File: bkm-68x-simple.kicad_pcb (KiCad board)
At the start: 2 copper layers, 232 x 233.5 mm, 138 parts, among them CN985 mezz-conn-02x50, CN986 mezz-conn-02x50, J1 Y_G, J10 TP_VIDEO_OE, J11 TP_VSYNC, J12 JTAG, J13 USB_A, J2 PB_B, J3 PR_R, J4 EXT_SYNC, J5 TP_Y_G, J6 TP_PB_B, J7 TP_PR_R, J8 TP_HSYNC, J9 TP_INT_EXT_SYNC, SW1 SW_DIP_x04, SW2 FORCE_VIDEO, U1 ADG1611, U10 74LVC541A, U11 BA33BC0FP-E2, U12 TC7SZ125FU, U13 LM2990SX-5.0, U14 BA50BC0FP-E2, U2 THS7374, U3 ISL59885, U4 ADG734, U5 74LVC14A, U6 74LVC14A, U7 74LVC14A, U8 TC7WH125, U9 MAX10-EVAL

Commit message: Minor fixes and cleanups
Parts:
- C18: value 22uF -> 330uF/LOW_ESR; footprint Capacitor_SMD:CP_Elec_6.3x5.4 -> Capacitor_SMD:CP_Elec_6.3x7.7
- C19, C25, C28: value 1uF -> 10uF
- C24: value 33uF/LOW_ESR -> 100uF
- C26: footprint Capacitor_SMD:CP_Elec_6.3x5.4 -> Capacitor_SMD:CP_Elec_6.3x7.7
- C29: footprint Capacitor_SMD:CP_Elec_6.3x5.4 -> Capacitor_SMD:CP_Elec_6.3x5.8
- moved R24 21.9 mm to (245.4, 191.7), turned to 180 degrees
- moved R28 21.8 mm to (245.4, 197.6), turned to 180 degrees
- moved R26 18.2 mm to (245.4, 193.7), turned to 180 degrees
- moved R27 14.4 mm to (245.4, 195.6), turned to 180 degrees
- moved R29 9.61 mm to (245.4, 199.5), turned to 180 degrees
- moved R30 5.92 mm to (245.4, 201.4), turned to 180 degrees
- moved R32 3.59 mm to (240.4, 203.5)
- moved R31 2.30 mm to (245.4, 203.4), turned to 180 degrees
- moved C21 1.38 mm to (239.1, 191.4), turned to 180 degrees
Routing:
- net Net-(R29-Pad2): track 36.3 -> 4.75 mm
- net Net-(R32-Pad2): track 34.0 -> 2.46 mm
- net Net-(R28-Pad2): track 35.3 -> 4.22 mm, vias 2 -> 0
- net Net-(R27-Pad2): track 34.4 -> 4.74 mm
- net Net-(R26-Pad2): track 35.7 -> 6.03 mm
- net Net-(R24-Pad2): track 35.8 -> 7.48 mm
- net Net-(R30-Pad2): track 33.2 -> 5.72 mm
- net Net-(R31-Pad2): track 34.2 -> 7.16 mm
- net AD5: track 54.0 -> 81.1 mm
- net AD4: track 52.6 -> 78.5 mm
- net AD6: track 53.6 -> 78.7 mm
- net AD1: track 55.5 -> 80.0 mm
- net AD7: track 54.6 -> 79.0 mm
- net AD3: track 53.0 -> 77.4 mm, vias 1 -> 3
- net AD2: track 55.4 -> 79.7 mm
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
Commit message: A lotta fixes
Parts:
- removed R44, R45: R, Resistor_SMD:R_0805_2012Metric_Pad1.20x1.40mm_HandSolder
- removed SW1: SW_DIP_x04, Button_Switch_SMD:SW_DIP_SPSTx04_Slide_9.78x12.34mm_W8.61mm_P2.54mm
- added R71: 47R, Resistor_SMD:R_0805_2012Metric_Pad1.20x1.40mm_HandSolder, F.Cu at (261.6, 86.6)
- added R72: 47R, Resistor_SMD:R_0805_2012Metric_Pad1.20x1.40mm_HandSolder, F.Cu at (260.7, 89.9)
- J1: value Y_G -> PR_R
- J2: value PB_B -> Y_G
- J3: value PR_R -> PB_B
- U10: footprint Housings_SSOP:TSSOP-20_4.4x6.5mm_Pitch0.65mm -> Package_SO:TSSOP-20_4.4x6.5mm_P0.65mm
- U12: footprint Package_TO_SOT_SMD:SOT-23-5_HandSoldering -> Package_TO_SOT_SMD:SOT-353_SC-70-5_Handsoldering
- U4: footprint Package_SO:TSSOP-16_4.4x5mm_P0.65mm -> Package_SO:TSSOP-20_4.4x6.5mm_P0.65mm
- moved R42 74.0 mm to (141.9, 202.7), turned to 0 degrees
- moved R43 73.1 mm to (142.4, 197.8), turned to 90 degrees
- moved J10 23.6 mm to (237.7, 89.3)
- moved C8 5.35 mm to (199.1, 107.6)
- moved C18 2.84 mm to (249.2, 173.2), turned to 90 degrees
- moved J13 1.81 mm to (199.1, 143.4)
- moved C9 1.26 mm to (211.1, 107.1), turned to 180 degrees
- moved U12 0.19 mm to (235.9, 241.9)
- moved J11 0.19 mm to (264.2, 89.9)
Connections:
- C3 pad 2: Y_G_IN -> PR_R_IN
- C4 pad 2: PB_B_IN -> Y_G_IN
- C5 pad 2: PR_R_IN -> PB_B_IN
- D1 pad 2: PB_B_IN -> Y_G_IN
- D2 pad 1: PB_B_IN -> Y_G_IN
- D3 pad 2: PR_R_IN -> PB_B_IN
- D4 pad 1: PR_R_IN -> PB_B_IN
- D5 pad 2: Y_G_IN -> PR_R_IN
- D6 pad 1: Y_G_IN -> PR_R_IN
- J1 pad 1: Y_G_IN -> PR_R_IN
- J2 pad 1: PB_B_IN -> Y_G_IN
- J3 pad 1: PR_R_IN -> PB_B_IN
- R1 pad 2: PB_B_IN -> Y_G_IN
- R2 pad 2: PR_R_IN -> PB_B_IN
- R3 pad 2: Y_G_IN -> PR_R_IN
- R42 pad 1: FORCE_VIDEO_BIT3 -> Net-(R42-Pad1)
- R42 pad 2: Net-(R42-Pad2) -> HSYNC_SEP
- R43 pad 1: FORCE_VIDEO_BIT2 -> VSYNC_SEP
- R5 pad 2: HSYNC_SEP -> Net-(R42-Pad1)
- R6 pad 1: VSYNC_SEP -> Net-(R43-Pad2)
- R7 pad 1: HSYNC_SEP -> Net-(R42-Pad1)
- R8 pad 1: VSYNC_SEP -> Net-(R43-Pad2)
- U2 pad 9: GND -> +5VA
- U8 pad 3: VSYNC -> Net-(R72-Pad1)
- U8 pad 6: HSYNC -> Net-(R71-Pad1)
- U9 pad 43: FORCE_VIDEO_BIT3 -> (no net)
- U9 pad 46: FORCE_VIDEO_BIT2 -> (no net)
- U9 pad 47: FORCE_VIDEO_BIT1 -> (no net)
- U9 pad 55: FORCE_VIDEO_BIT0 -> (no net)
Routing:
- net HSYNC_SEP: track 150.3 -> 3.26 mm
- net Net-(R42-Pad1): track 0.00 -> 145.9 mm
- net VSYNC_SEP: track 143.1 -> 4.66 mm
- net Net-(R43-Pad2): track 8.01 -> 137.3 mm
- net FORCE_VIDEO_BIT2: track 89.1 -> 0.00 mm
- net FORCE_VIDEO_BIT3: track 89.1 -> 0.00 mm
- net FORCE_VIDEO_BIT1: track 89.1 -> 0.00 mm
- net FORCE_VIDEO_BIT0: track 89.1 -> 0.00 mm
- net +3V3: track 374.8 -> 363.1 mm, vias 11 -> 10
- net VSYNC: track 25.3 -> 16.9 mm
- net PR_R_IN: track 125.0 -> 133.1 mm
- net Net-(R45-Pad2): track 8.05 -> 0.00 mm
- net Net-(R44-Pad2): track 8.03 -> 0.00 mm
- net Net-(R42-Pad2): track 8.03 -> 0.00 mm
- net Y_G_IN: track 133.1 -> 125.8 mm
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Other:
- board text added: "PB/B (BLUE)"
- board text added: "PR/R (RED)"
- board text added: "Rev. A"
- board text added: "SYNC (YELLOW) Max 5Vpp"
- board text added: "Y/G (GREEN)"
- board text removed: "USB"

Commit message: Onboard FPGA, passthroughs and a lot of other stuff
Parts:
- added C30: 0.1uF, Capacitor_SMD:C_0603_1608Metric_Pad1.08x0.95mm_HandSolder, F.Cu at (213.0, 207.9)
- added C31: 0.1uF, Capacitor_SMD:C_0603_1608Metric_Pad1.08x0.95mm_HandSolder, F.Cu at (212.9, 211.2)
- added C32: 0.1uF, Capacitor_SMD:C_0603_1608Metric_Pad1.08x0.95mm_HandSolder, F.Cu at (212.7, 214.5)
- added C33: 0.1uF, Capacitor_SMD:C_0603_1608Metric_Pad1.08x0.95mm_HandSolder, F.Cu at (208.8, 219.8)
- added C34: 0.1uF, Capacitor_SMD:C_0603_1608Metric_Pad1.08x0.95mm_HandSolder, F.Cu at (210.3, 204.8)
- added C35: 0.1uF, Capacitor_SMD:C_0603_1608Metric_Pad1.08x0.95mm_HandSolder, F.Cu at (201.9, 196.6)
- added C36: 0.1uF, Capacitor_SMD:C_0603_1608Metric_Pad1.08x0.95mm_HandSolder, F.Cu at (206.1, 200.6)
- added C37: 0.1uF, Capacitor_SMD:C_0603_1608Metric_Pad1.08x0.95mm_HandSolder, F.Cu at (198.7, 194.6)
- added C38: 0.1uF, Capacitor_SMD:C_0603_1608Metric_Pad1.08x0.95mm_HandSolder, F.Cu at (190.3, 198.9)
- added C39: 0.1uF, Capacitor_SMD:C_0603_1608Metric_Pad1.08x0.95mm_HandSolder, F.Cu at (196.3, 194.5)
- added C40: 0.1uF, Capacitor_SMD:C_0603_1608Metric_Pad1.08x0.95mm_HandSolder, F.Cu at (185.5, 202.7)
- added C41: 0.1uF, Capacitor_SMD:C_0603_1608Metric_Pad1.08x0.95mm_HandSolder, F.Cu at (203.5, 223.5)
- added C42: 0.1uF, Capacitor_SMD:C_0603_1608Metric_Pad1.08x0.95mm_HandSolder, F.Cu at (200.3, 226.7)
- added C43: 0.1uF, Capacitor_SMD:C_0603_1608Metric_Pad1.08x0.95mm_HandSolder, F.Cu at (182.0, 215.6)
- added C44: 0.1uF, Capacitor_SMD:C_0603_1608Metric_Pad1.08x0.95mm_HandSolder, F.Cu at (185.9, 219.4)
- added C45: 0.1uF, Capacitor_SMD:C_0603_1608Metric_Pad1.08x0.95mm_HandSolder, F.Cu at (180.8, 214.5)
- added C46: 0.1uF, Capacitor_SMD:C_0603_1608Metric_Pad1.08x0.95mm_HandSolder, F.Cu at (180.5, 210.4)
- added C47: 0.1uF, Capacitor_SMD:C_0603_1608Metric_Pad1.08x0.95mm_HandSolder, F.Cu at (193.2, 226.9)
- added C48: 0.1uF, Capacitor_SMD:C_0603_1608Metric_Pad1.08x0.95mm_HandSolder, F.Cu at (191.3, 224.9)
- added C49: 0.1uF, Capacitor_SMD:C_0603_1608Metric_Pad1.08x0.95mm_HandSolder, F.Cu at (182.1, 206.7)
- added C50: 10pF, Capacitor_SMD:C_0603_1608Metric_Pad1.08x0.95mm_HandSolder, F.Cu at (185.2, 197.7)
- added C51: 10pF, Capacitor_SMD:C_0603_1608Metric_Pad1.08x0.95mm_HandSolder, F.Cu at (176.0, 201.1)
- added C52: 10pF, Capacitor_SMD:C_0603_1608Metric_Pad1.08x0.95mm_HandSolder, F.Cu at (188.4, 194.5)
- added C53: 10pF, Capacitor_SMD:C_0603_1608Metric_Pad1.08x0.95mm_HandSolder, F.Cu at (183.5, 199.4)
- added C54: 100pF, Capacitor_SMD:C_0805_2012Metric_Pad1.18x1.45mm_HandSolder, F.Cu at (202.3, 109.2)
- added C55: 470pF, Capacitor_SMD:C_0805_2012Metric_Pad1.18x1.45mm_HandSolder, F.Cu at (204.6, 109.2)
- added C56: 0.1uF, Capacitor_SMD:C_0805_2012Metric_Pad1.18x1.45mm_HandSolder, F.Cu at (262.0, 108.5)
- added C57: 0.1uF, Capacitor_SMD:C_0805_2012Metric_Pad1.18x1.45mm_HandSolder, F.Cu at (236.9, 111.2)
- added C58: 100uF, Capacitor_SMD:CP_Elec_6.3x5.4, F.Cu at (207.7, 187.4)
- added C59: 0.1uF, Capacitor_SMD:C_0805_2012Metric_Pad1.18x1.45mm_HandSolder, F.Cu at (204.5, 183.8)
- added D10: D_Schottky, Diode_SMD:D_SOD-123, F.Cu at (177.4, 199.7)
- added D11: D_Schottky, Diode_SMD:D_SOD-123, F.Cu at (185.4, 191.6)
- added D12: D_Schottky, Diode_SMD:D_SOD-123, F.Cu at (180.6, 196.5)
- added D13: DEBUG1, LED_SMD:LED_0805_2012Metric_Pad1.15x1.40mm_HandSolder, F.Cu at (182.0, 226.8)
- added D14: DEBUG2, LED_SMD:LED_0805_2012Metric_Pad1.15x1.40mm_HandSolder, F.Cu at (183.5, 228.4)
- added D9: D_Schottky, Diode_SMD:D_SOD-123, F.Cu at (182.3, 194.7)
- added J14: JTAG, Connector_PinHeader_2.54mm:PinHeader_2x05_P2.54mm_Vertical, F.Cu at (172.2, 193.5)
- added J15: Y_G_OUT, BNC-THT:BNC-THT, F.Cu at (57.8, 126.6)
- added J16: PB_B_OUT, BNC-THT:BNC-THT, F.Cu at (57.8, 166.7)
- added J17: EXT_SYNC_OUT, BNC-THT:BNC-THT, F.Cu at (57.7, 206.8)
- added Q1: MMBT3904, Package_TO_SOT_SMD:SOT-23_Handsoldering, F.Cu at (207.7, 110.0)
- added R44: 10K, Resistor_SMD:R_0805_2012Metric_Pad1.20x1.40mm_HandSolder, F.Cu at (205.6, 198.6)
- added R45: 10K, Resistor_SMD:R_0805_2012Metric_Pad1.20x1.40mm_HandSolder, F.Cu at (205.4, 194.8)
- added R73: 10K, Resistor_SMD:R_0805_2012Metric_Pad1.20x1.40mm_HandSolder, F.Cu at (204.0, 193.4)
- added R74: 10K, Resistor_SMD:R_0805_2012Metric_Pad1.20x1.40mm_HandSolder, F.Cu at (179.1, 198.2)
- added R75: 10K, Resistor_SMD:R_0805_2012Metric_Pad1.20x1.40mm_HandSolder, F.Cu at (187.0, 189.9)
- added R76: 1K, Resistor_SMD:R_0805_2012Metric_Pad1.20x1.40mm_HandSolder, F.Cu at (183.9, 193.2)
- added R77: 10K, Resistor_SMD:R_0805_2012Metric_Pad1.20x1.40mm_HandSolder, F.Cu at (182.0, 220.9)
- added R78: 22R, Resistor_SMD:R_0805_2012Metric_Pad1.20x1.40mm_HandSolder, F.Cu at (213.6, 194.3)
- added R79: 22R, Resistor_SMD:R_0805_2012Metric_Pad1.20x1.40mm_HandSolder, F.Cu at (211.1, 191.0)
- added R80: 100R, Resistor_SMD:R_0805_2012Metric_Pad1.20x1.40mm_HandSolder, F.Cu at (198.3, 110.9)
- added R81: 10K, Resistor_SMD:R_0805_2012Metric_Pad1.20x1.40mm_HandSolder, F.Cu at (206.8, 115.0)
- added R82: 470R, Resistor_SMD:R_0805_2012Metric_Pad1.20x1.40mm_HandSolder, F.Cu at (184.9, 223.9)
- added R83: 470R, Resistor_SMD:R_0805_2012Metric_Pad1.20x1.40mm_HandSolder, F.Cu at (186.4, 225.4)
- added SW1: FORCE_VIDEO, PTS645:PTS645, F.Cu at (53.3, 240.1)
- added SW3: PR_R_TERM, JS202011SCQN:JS202011SCQN, F.Cu at (77.2, 66.7)
- added SW4: Y_G_TERM, JS202011SCQN:JS202011SCQN, F.Cu at (77.1, 106.7)
- added SW5: PB_B_TERM, JS202011SCQN:JS202011SCQN, F.Cu at (77.0, 146.6)
- added SW6: EXT_SYNC_TERM, JS202011SCQN:JS202011SCQN, F.Cu at (77.0, 186.7)
- added U15: 10M08SC, Package_QFP:EQFP-144-1EP_20x20mm_P0.5mm_EP8.93x8.7mm_ThermalVias, F.Cu at (196.8, 210.9)
- C11: value 0.1uF -> 56nF
- C27: value C -> 0.1uF
- J13: value USB_A -> PR_R_OUT; footprint Connector_USB:USB_A_Molex_67643_Horizontal -> BNC-THT:BNC-THT
- R42, R43: value R -> 47R
- R46: value R -> 10K
- R5, R6, R7, R8: value R -> 1K
- U9: value MAX10-EVAL -> KC2520Z50; footprint max10-eval:max-10-eval -> Oscillator:Oscillator_SMD_Kyocera_KC2520Z-4Pin_2.5x2.0mm
- moved J13 152.0 mm to (58.0, 86.7), turned to 0 degrees
- moved C27 147.3 mm to (206.6, 122.2)
- moved R46 122.6 mm to (180.6, 219.4), turned to 225 degrees
- moved D8 60.1 mm to (69.9, 190.6)
- moved J4 60.0 mm to (57.7, 186.7)
- moved D7 60.0 mm to (69.9, 185.0)
- moved SW2 55.7 mm to (53.3, 229.8)
- moved R42 54.8 mm to (194.7, 187.8), turned to 225 degrees
- moved R43 52.1 mm to (193.2, 186.2), turned to 45 degrees
- moved R4 50.0 mm to (77.0, 180.6), turned to 0 degrees
- moved U9 47.0 mm to (182.0, 203.1), turned to 45 degrees
- moved D4 40.0 mm to (69.9, 150.6)
- moved J3 39.9 mm to (57.8, 146.6)
- moved D3 39.9 mm to (69.9, 145.0)
- moved R2 30.1 mm to (77.0, 140.5), turned to 0 degrees
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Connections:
- C10 pad 2: SYNC_SRC -> SYNC_SRC_FILTER
- C27 pad 1: FORCE_VIDEO -> +5VA
- J13 pad 1: STBY_5V -> Net-(J13-Pad1)
- J13 pad 2: (no net) -> GND
- R1 pad 1: GND -> Net-(R1-Pad1)
- R1 pad 2: Y_G_IN -> GND
- R2 pad 1: GND -> Net-(R2-Pad1)
- R2 pad 2: PB_B_IN -> GND
- R3 pad 1: GND -> Net-(R3-Pad1)
- R3 pad 2: PR_R_IN -> GND
- R4 pad 1: GND -> Net-(R4-Pad1)
- R4 pad 2: EXT_SYNC_IN -> GND
- R46 pad 2: Net-(R46-Pad2) -> +3V3
- SW2 pad 1: Net-(R46-Pad2) -> FORCE_VIDEO
- SW2 pad 2: +3V3 -> GND
- U1 pad 11: (no net) -> GND
- U1 pad 9: (no net) -> GND
- U3 pad 5: (no net) -> /Video/ISL_SD_HD
- U4 pad 10: (no net) -> GND
- U4 pad 11: (no net) -> GND
- U4 pad 12: (no net) -> GND
- U4 pad 14: (no net) -> GND
- U4 pad 17: (no net) -> GND
- U4 pad 19: (no net) -> GND
- U4 pad 20: (no net) -> GND
- U4 pad 7: (no net) -> GND
- U4 pad 9: (no net) -> GND
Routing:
- net +5VA: track 365.5 -> 532.4 mm
- net FORCE_VIDEO2: track 0.00 -> 146.7 mm
- net +3V3: track 363.1 -> 457.5 mm, vias 10 -> 21
- net STBY_5V: track 159.3 -> 69.1 mm
- net Net-(R42-Pad1): track 145.9 -> 67.2 mm
- net INT_~EXT~_SYNC: track 187.6 -> 113.2 mm, vias 2 -> 4
- net Net-(R43-Pad2): track 137.3 -> 67.2 mm
- net GND: track 97.6 -> 166.5 mm, vias 28 -> 53
- net VSYNC_OUT: track 180.1 -> 130.1 mm
- net HSYNC_OUT: track 176.3 -> 130.0 mm
- net FORCE_VIDEO: track 97.6 -> 140.3 mm
- net PB_B_IN: track 125.0 -> 158.7 mm
- net Y_G_IN: track 125.8 -> 158.5 mm
- net /FPGA/TCK: track 0.00 -> 27.9 mm
- net /FPGA/TMS: track 0.00 -> 27.4 mm
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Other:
- outline, holes or cut-outs redrawn
- board text added: "BKM-68X Alternative (SKM-69X) (2021) Martin Hejnfelt www.immerhax.com"
- board text added: "DBG1"
- board text added: "DBG2"
- board text added: "EXT. SYNC (YELLOW) Max 5Vpp"
- board text added: "EXT. SYNC OUT"
- board text added: "PB/B OUT"
- board text added: "PR/R OUT"
- board text added: "Rev. B"
- board text added: "UP = 75R TERM DOWN = PASSTHROUGH"
- board text added: "Y/G OUT"
- board text removed: "5V power only for FPGA"
- board text removed: "Altera/Intel MAX10 10M08S Evaluation Kit"
- board text removed: "BKM-68X Alternative (2021) Martin Hejnfelt www.immerhax.com"
- board text removed: "Rev. A"
- board text removed: "SYNC (YELLOW) Max 5Vpp"

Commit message: Updated some component values
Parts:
- R15, R16, R17, R18, R19, R20, R21, R22, R23, R25, R36, R38, R47, R48, R49, R50, R51, R52, R53, R62, R63, R64, R65, R66, R67: value 68 -> 68R
- R24, R26, R27, R28, R29, R30, R31, R32: value 47 -> 47R
- R40, R41, R54, R55, R56, R57, R58, R59, R60, R61, R68, R69, R70: value 22 -> 22R
- R83: value 470R -> 390R

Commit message: Fixes and additions
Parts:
- added C60: 0.1uF, Capacitor_SMD:C_0603_1608Metric_Pad1.08x0.95mm_HandSolder, F.Cu at (184.7, 218.3)
- added H1: SCREWMOUNT_90DEG, keystone-7794:7794-X, F.Cu at (57.5, 255.0)
- added H2: SCREWMOUNT_90DEG, keystone-7794:7794-X, F.Cu at (57.5, 45.0)
- moved C28 12.6 mm to (245.5, 100.5)
- moved C25 4.21 mm to (249.1, 120.4), turned to 270 degrees
- moved C19 1.74 mm to (253.8, 174.3), turned to 90 degrees
- moved C16 1.65 mm to (258.1, 126.7)
- moved C17 1.65 mm to (253.3, 126.4)
- moved C46 0.41 mm to (180.7, 210.7)
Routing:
- net -6V: track 118.9 -> 116.5 mm
- net +3V3: track 457.5 -> 459.9 mm
- net +6V: track 100.1 -> 98.7 mm
- net +5VA: track 532.4 -> 532.9 mm
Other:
- board text added: "Rev. C"
- board text removed: "Rev. B"

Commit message: Shortened board slightly for PCB front, rev C
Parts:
- moved J4 1.72 mm to (59.4, 186.6)
- moved J17 1.71 mm to (59.4, 206.6)
- moved J16 1.66 mm to (59.4, 166.6)
- moved J3 1.65 mm to (59.4, 146.6)
- moved J15 1.65 mm to (59.4, 126.6)
- moved H2 1.63 mm to (59.1, 45.0)
- moved H1 1.63 mm to (59.1, 255.0)
- moved SW2 1.51 mm to (54.8, 229.8)
- moved SW1 1.50 mm to (54.8, 240.1)
- moved J2 1.40 mm to (59.4, 106.7)
- moved J1 1.30 mm to (59.3, 66.7)
- moved J13 1.17 mm to (59.2, 86.7)
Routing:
- net Net-(J17-Pad1): track 25.0 -> 23.2 mm
- net EXT_SYNC_IN: track 157.9 -> 156.2 mm
- net Net-(J16-Pad1): track 25.3 -> 23.6 mm
- net Net-(J15-Pad1): track 25.4 -> 23.8 mm
- net PB_B_IN: track 158.7 -> 157.1 mm
- net FORCE_VIDEO: track 140.3 -> 138.8 mm
- net FORCE_VIDEO2: track 146.6 -> 145.1 mm
- net Net-(J13-Pad1): track 26.1 -> 24.7 mm
- net PR_R_IN: track 158.7 -> 157.3 mm
- net Y_G_IN: track 158.5 -> 157.1 mm
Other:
- board size 232 x 233.5 mm -> 230.4 x 233.5 mm

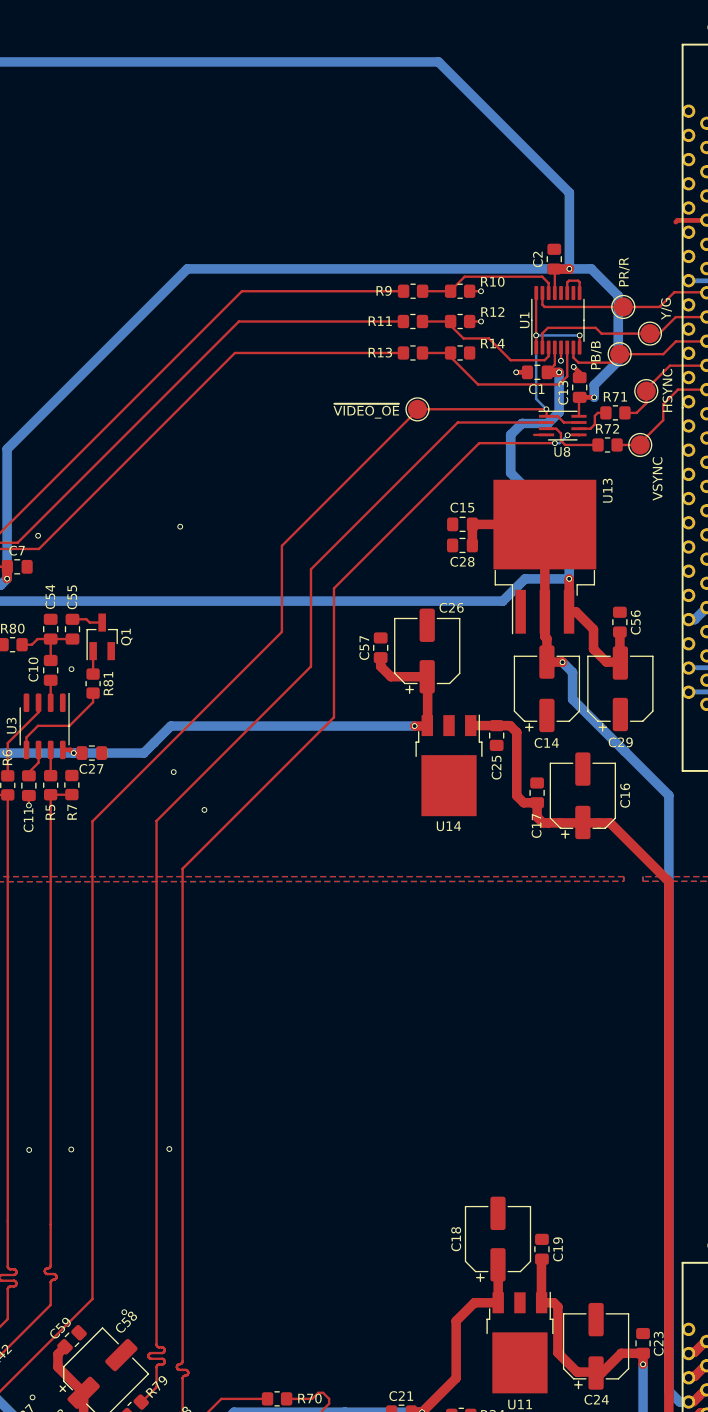
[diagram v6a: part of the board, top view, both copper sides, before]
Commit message: Replace ADG1611BRUZ with BCPZ
Should also be compatible with Vishay DG1411EEN-T1-GE4
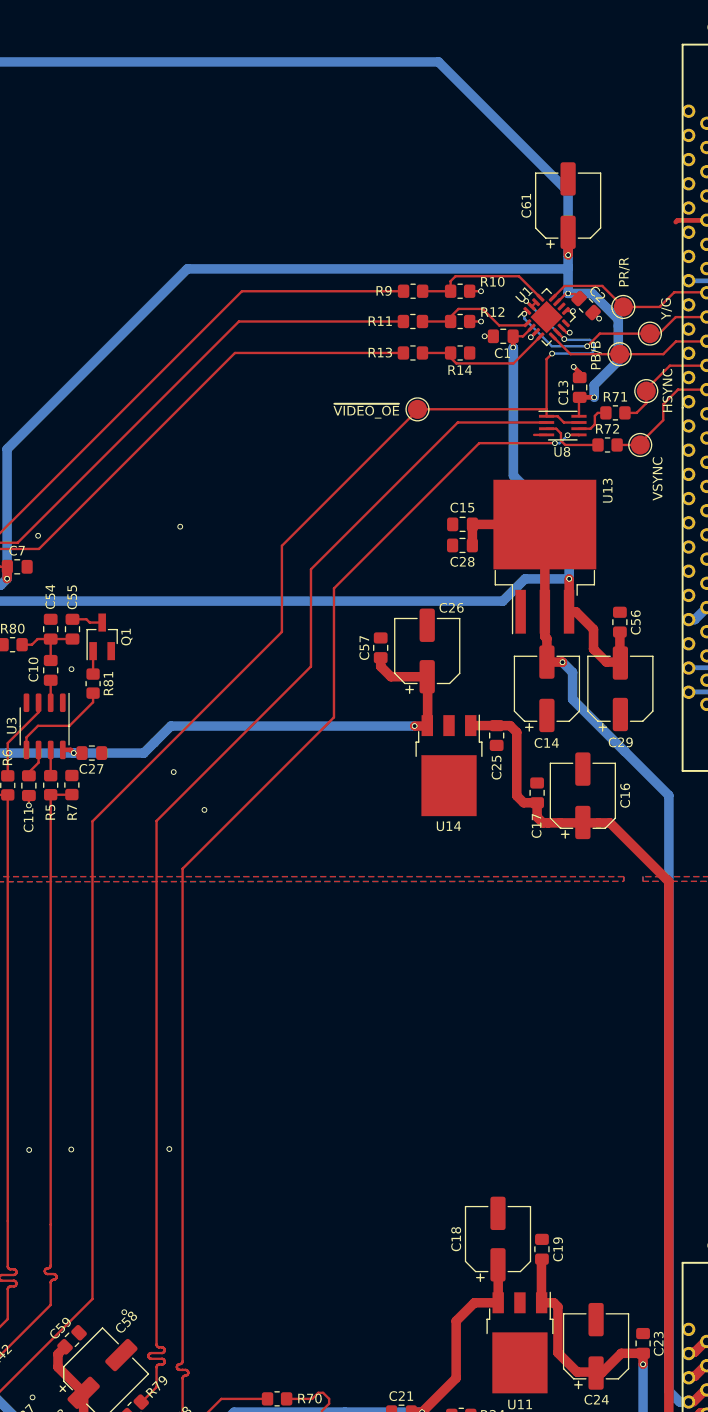
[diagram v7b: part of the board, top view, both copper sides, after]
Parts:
- added C61: 100uF, Capacitor_SMD:CP_Elec_6.3x5.3, F.Cu at (256.6, 64.8)
- U1: value ADG1611 -> ADG1611BCPZ; footprint Package_SO:TSSOP-16_4.4x5mm_P0.65mm -> Package_CSP:LFCSP-16-1EP_4x4mm_P0.65mm_EP2.4x2.4mm
- moved C2 5.90 mm to (258.5, 75.3), turned to 315 degrees
- moved C1 5.21 mm to (249.8, 78.5)
- moved U1 1.23 mm to (254.3, 76.5), turned to 45 degrees
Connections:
- U1 pad 1: ~VIDEO_OE -> Net-(R11-Pad2)
- U1 pad 11: GND -> +5VA
- U1 pad 12: (no net) -> PR_R
- U1 pad 13: +5VA -> Net-(R10-Pad2)
- U1 pad 14: Net-(R10-Pad2) -> ~VIDEO_OE
- U1 pad 15: PR_R -> ~VIDEO_OE
- U1 pad 16: ~VIDEO_OE -> Y_G
- U1 pad 2: Y_G -> -5VA
- U1 pad 3: Net-(R11-Pad2) -> GND
- U1 pad 4: -5VA -> Net-(R13-Pad2)
- U1 pad 5: GND -> PB_B
- U1 pad 6: Net-(R13-Pad2) -> ~VIDEO_OE
- U1 pad 7: PB_B -> GND
- U1 pad 8: ~VIDEO_OE -> (no net)
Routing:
- net Net-(R13-Pad2): track 20.2 -> 14.3 mm
- net Net-(R11-Pad2): track 16.3 -> 12.6 mm
- net ~VIDEO_OE: track 202.4 -> 205.5 mm
- net Y_G: track 22.9 -> 25.5 mm, vias 0 -> 2
- net -5VA: track 116.1 -> 114.3 mm
- net GND: track 166.5 -> 164.7 mm, vias 53 -> 56
- net PB_B: track 20.6 -> 21.9 mm
- net PR_R: track 23.1 -> 22.1 mm
- net +5VA: track 532.9 -> 533.8 mm, vias 10 -> 11
- net Net-(R10-Pad2): track 15.2 -> 14.6 mm

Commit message: Rev C1
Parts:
- R11, R13, R9: value 75R -> 150R
- R42, R43: value 47R -> 68R
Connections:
- U1 pad 17: (no net) -> -5VA
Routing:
- net -5VA: track 114.3 -> 116.3 mm
- net GND: vias 56 -> 57
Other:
- board text added: "Rev. C1"
- board text removed: "Rev. C"
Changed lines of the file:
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@@
     (thickness 1.6)
     (drawings 40)
-    (tracks 7545)
+    (tracks 7549)
     (zones 0)
     (modules 201)
@@
   )
   (setup
-    (last_trace_width 1)
+    (last_trace_width 0.25)
     (user_trace_width 0.5)
     (user_trace_width 1)
@@
       (drillshape 0)
       (scaleselection 1)
-      (outputdirectory "plot_revc"))
+      (outputdirectory "plot"))
   )
   (net 0 "")
@@
     (pad 16 smd roundrect (at -0.975 -1.8875 45) (size 0.35 0.975) (layers F.Cu F.Paste F.Mask) (roundrect_rratio 0.25)
       (net 19 Y_G))
-    (pad 17 smd rect (at 0 0 45) (size 2.4 2.4) (layers F.Cu F.Mask))
+    (pad 17 smd rect (at 0 0 45) (size 2.4 2.4) (layers F.Cu F.Mask)
+      (net 134 -5VA))
     (pad "" smd roundrect (at -0.6 -0.6 45) (size 0.97 0.97) (layers F.Paste) (roundrect_rratio 0.25))
     (pad "" smd roundrect (at -0.6 0.6 45) (size 0.97 0.97) (layers F.Paste) (roundrect_rratio 0.25))
@@
       (effects (font (size 1 1) (thickness 0.15)))
     )
-    (fp_text value 75R (at 0 1.65) (layer F.Fab)
+    (fp_text value 150R (at 0 1.65) (layer F.Fab)
       (effects (font (size 1 1) (thickness 0.15)))
     )
@@
       (effects (font (size 1 1) (thickness 0.15)))
     )
-    (fp_text value 75R (at 0 1.65) (layer F.Fab)
+    (fp_text value 150R (at 0 1.65) (layer F.Fab)
       (effects (font (size 1 1) (thickness 0.15)))
     )
@@
       (effects (font (size 1 1) (thickness 0.15)))
     )
-    (fp_text value 75R (at 0 1.65) (layer F.Fab)
+    (fp_text value 150R (at 0 1.65) (layer F.Fab)
       (effects (font (size 1 1) (thickness 0.15)))
     )
@@
       (effects (font (size 1 1) (thickness 0.15)))
     )
-    (fp_text value 47R (at 0.05967 -1.670328 45) (layer F.Fab)
+    (fp_text value 68R (at 0.05967 -1.670328 45) (layer F.Fab)
       (effects (font (size 1 1) (thickness 0.15)))
     )
@@
       (effects (font (size 1 1) (thickness 0.15)))
     )
-    (fp_text value 47R (at -0.066054 -1.580525 45) (layer F.Fab)
+    (fp_text value 68R (at -0.066054 -1.580525 45) (layer F.Fab)
       (effects (font (size 1 1) (thickness 0.15)))
     )
@@
     (effects (font (size 3 3) (thickness 0.65)) (justify left))
   )
-  (gr_text "Rev. C" (at 56.94 264.4) (layer F.SilkS)
+  (gr_text "Rev. C1" (at 56.94 264.4) (layer F.SilkS)
     (effects (font (size 1.5 1.5) (thickness 0.3)))
   )
@@
   (gr_line (start 281.94 266.7) (end 281.94 33.2) (layer Edge.Cuts) (width 0.15))
   (segment (start 204.566303 203.520751) (end 204.581049 203.520751) (width 0.25) (layer F.Cu) (net 0))
+  (via (at 228.5655 75.4148) (size 0.6) (drill 0.4) (layers F.Cu B.Cu) (net 1))
   (via (at 204.4954 113.4364) (size 0.6) (drill 0.4) (layers F.Cu B.Cu) (net 1))
   (via (at 215.9 98.4885) (size 0.6) (drill 0.4) (layers F.Cu B.Cu) (net 1))
@@
   (segment (start 256.7051 98.9838) (end 256.7051 103.9622) (width 1) (layer B.Cu) (net 134))
   (segment (start 250.8247 79.6914) (end 250.85146 79.71816) (width 1) (layer B.Cu) (net 134))
+  (segment (start 252.775526 77.604854) (end 252.775526 77.595374) (width 0.25) (layer F.Cu) (net 134))
+  (segment (start 253.8709 76.5) (end 254.34 76.5) (width 0.25) (layer F.Cu) (net 134))
+  (segment (start 252.775526 77.595374) (end 253.8709 76.5) (width 0.25) (layer F.Cu) (net 134))
   (segment (start 204.51496 126.61138) (end 204.53096 126.59538) (width 0.25) (layer F.Cu) (net 135))
   (segment (start 202.30846 126.61138) (end 204.51496 126.61138) (width 0.25) (layer F.Cu) (net 135))
